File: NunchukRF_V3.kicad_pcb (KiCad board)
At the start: 2 copper layers, 26.9 x 46.7 mm, 43 parts, among them K1 Buttons, P1 V+, P2 V-, P3 D-, P4 Vbat-, P5 Vbat+, P6 D+, Q1 MOSFET_N, Q2 MOSFET_P, U1 STM32F100C6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

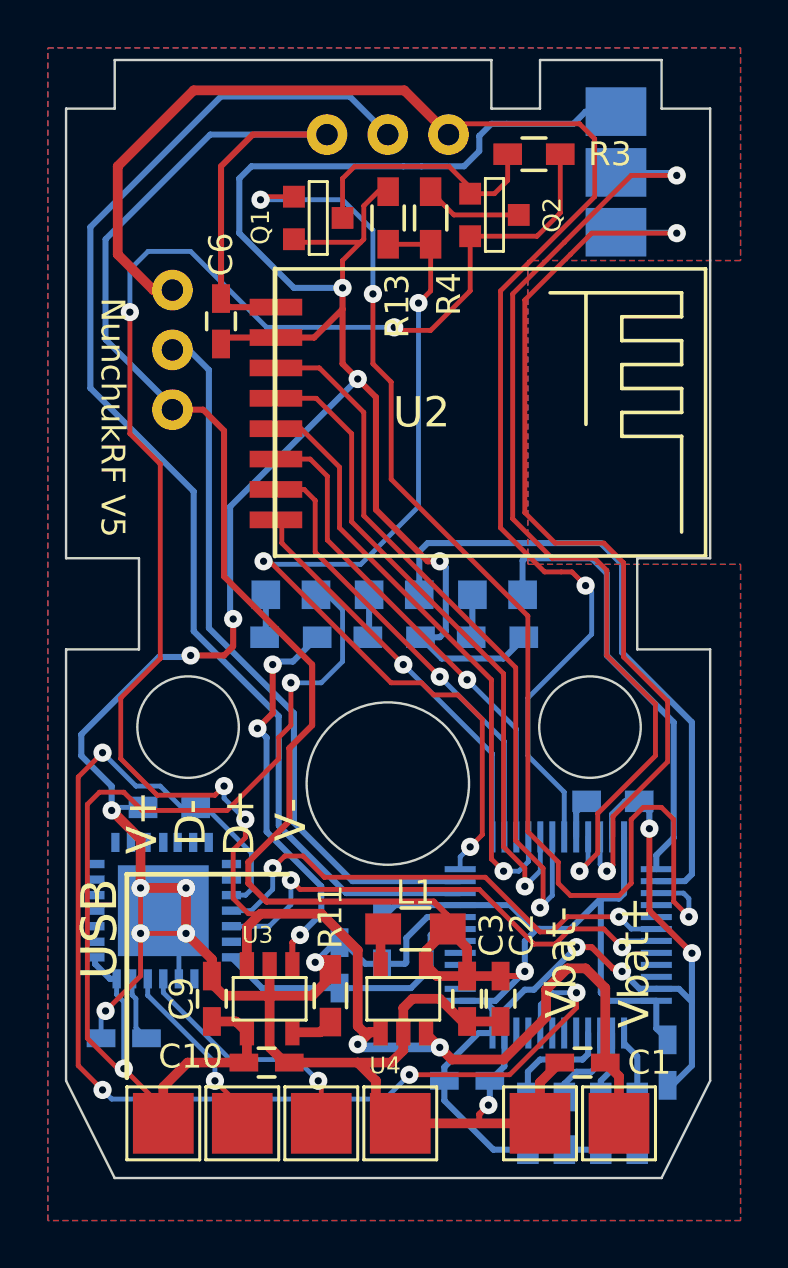
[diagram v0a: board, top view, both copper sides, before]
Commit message: Added cp2102 power detect connection to mcu
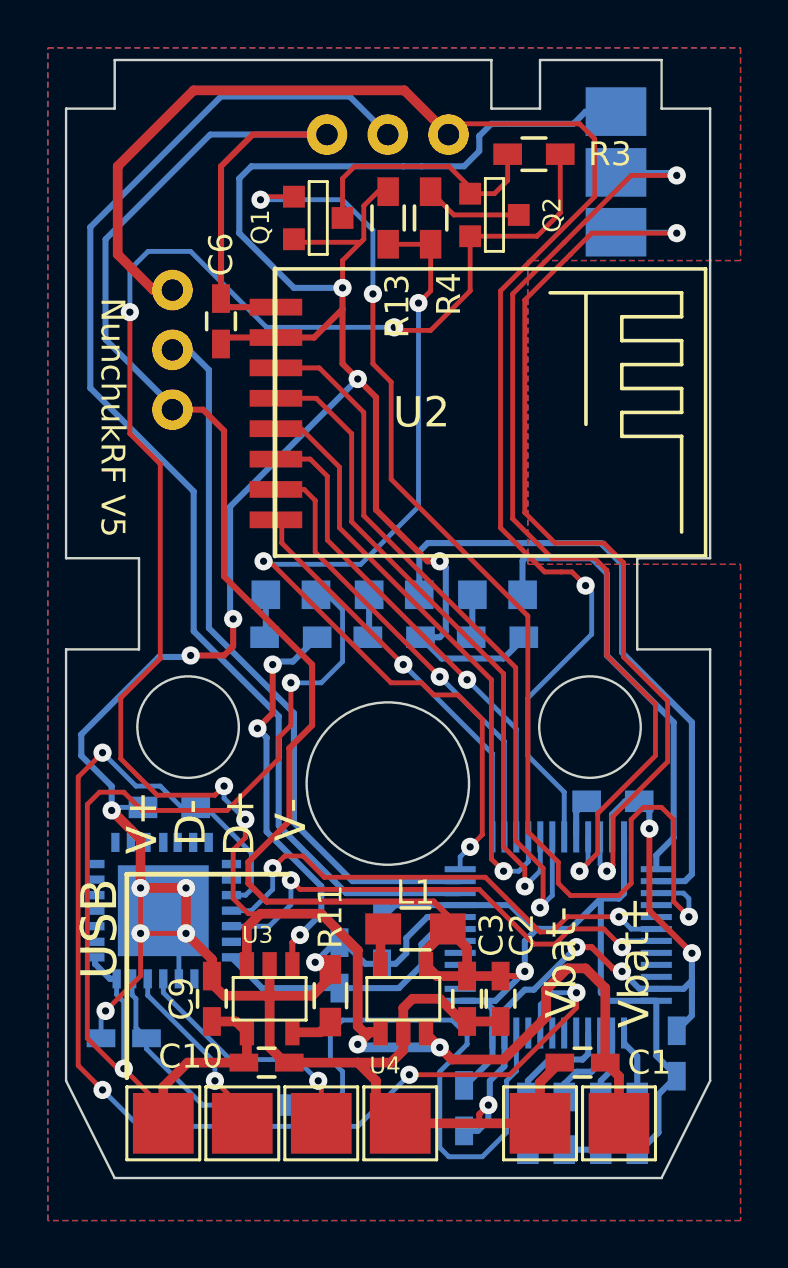
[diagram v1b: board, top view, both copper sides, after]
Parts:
- added R14: 2k, Resistors_SMD:R_0603_HandSoldering, B.Cu at (224.3, 88.4)
- moved C7 1.15 mm to (232.5, 88.5), turned to 90 degrees
- moved C5 0.54 mm to (241.4, 86.2), turned to 270 degrees
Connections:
- net Net-(C11-Pad2) renamed CP2102_ON
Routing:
- net Net-(R14-Pad2): track 0.00 -> 24.1 mm
- net CP2102_ON: track 2.73 -> 8.07 mm
- net GND: track 193.2 -> 192.2 mm
- net BOOT0: track 50.4 -> 51.4 mm
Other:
- board text added: "Addr b0 - b3"
- board text removed: "Address b0 - b3"

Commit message: Updated NRF labels
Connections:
- U1 pad 13: NRF_CE -> NRF_IRQ
- U1 pad 14: NRF_CSN -> NRF_MISO
- U1 pad 15: NRF_SCK -> NRF_MOSI
- U1 pad 16: NRF_MOSI -> NRF_SCK
- U1 pad 17: NRF_MISO -> NRF_CSN
- U1 pad 18: NRF_IRQ -> NRF_CE
- U1 pad 2: Net-(U1-Pad2) -> (no net)
- U1 pad 28: Net-(U1-Pad28) -> (no net)
- U1 pad 29: Net-(U1-Pad29) -> (no net)
- U1 pad 3: Net-(U1-Pad3) -> (no net)
- U1 pad 32: Net-(U1-Pad32) -> (no net)
- U1 pad 33: Net-(U1-Pad33) -> (no net)
- U1 pad 34: Net-(U1-Pad34) -> (no net)
- U1 pad 4: Net-(U1-Pad4) -> (no net)
- U1 pad 41: Net-(U1-Pad41) -> (no net)
- U1 pad 42: Net-(U1-Pad42) -> (no net)
- U1 pad 43: Net-(U1-Pad43) -> (no net)
- U1 pad 45: Net-(U1-Pad45) -> (no net)
- U1 pad 5: Net-(U1-Pad5) -> (no net)
- U1 pad 6: Net-(U1-Pad6) -> (no net)
- U2 pad 3: NRF_IRQ -> NRF_CE
- U2 pad 4: NRF_MISO -> NRF_CSN
- U2 pad 5: NRF_MOSI -> NRF_SCK
- U2 pad 6: NRF_SCK -> NRF_MOSI
- U2 pad 7: NRF_CSN -> NRF_MISO
- U2 pad 8: NRF_CE -> NRF_IRQ
- U5 pad 1: Net-(U5-Pad1) -> (no net)
- U5 pad 11: Net-(U5-Pad11) -> (no net)
- U5 pad 12: Net-(U5-Pad12) -> (no net)
- U5 pad 18: Net-(U5-Pad18) -> (no net)
- U5 pad 2: Net-(U5-Pad2) -> (no net)
- U5 pad 23: Net-(U5-Pad23) -> (no net)
- U5 pad 27: Net-(U5-Pad27) -> (no net)
- U5 pad 9: Net-(U5-Pad9) -> (no net)
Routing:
- net NRF_CE: track 17.0 -> 31.5 mm
- net NRF_IRQ: track 31.5 -> 17.0 mm
- net NRF_MISO: track 28.0 -> 19.2 mm
- net NRF_CSN: track 19.2 -> 28.0 mm
- net NRF_SCK: track 20.8 -> 25.3 mm
- net NRF_MOSI: track 25.3 -> 20.8 mm

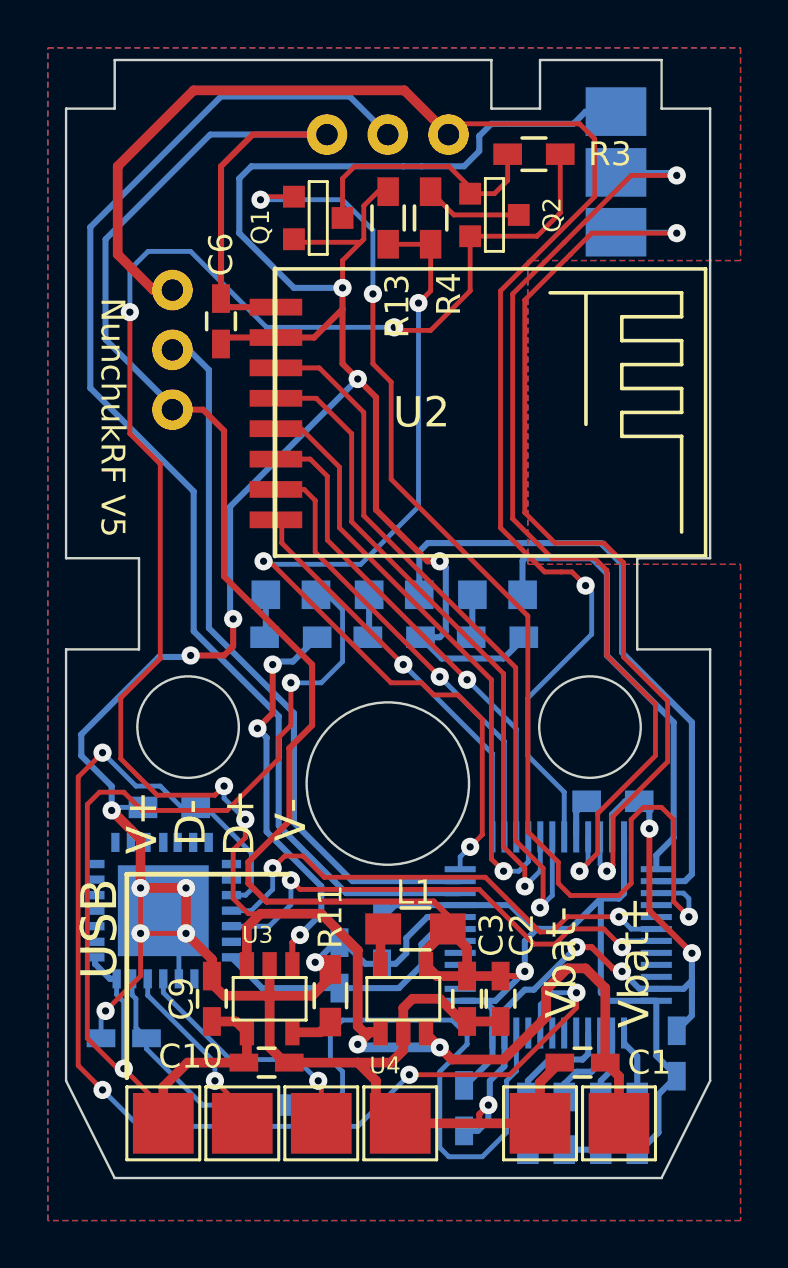
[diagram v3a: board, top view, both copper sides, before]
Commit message: Changed CP2102 footprint
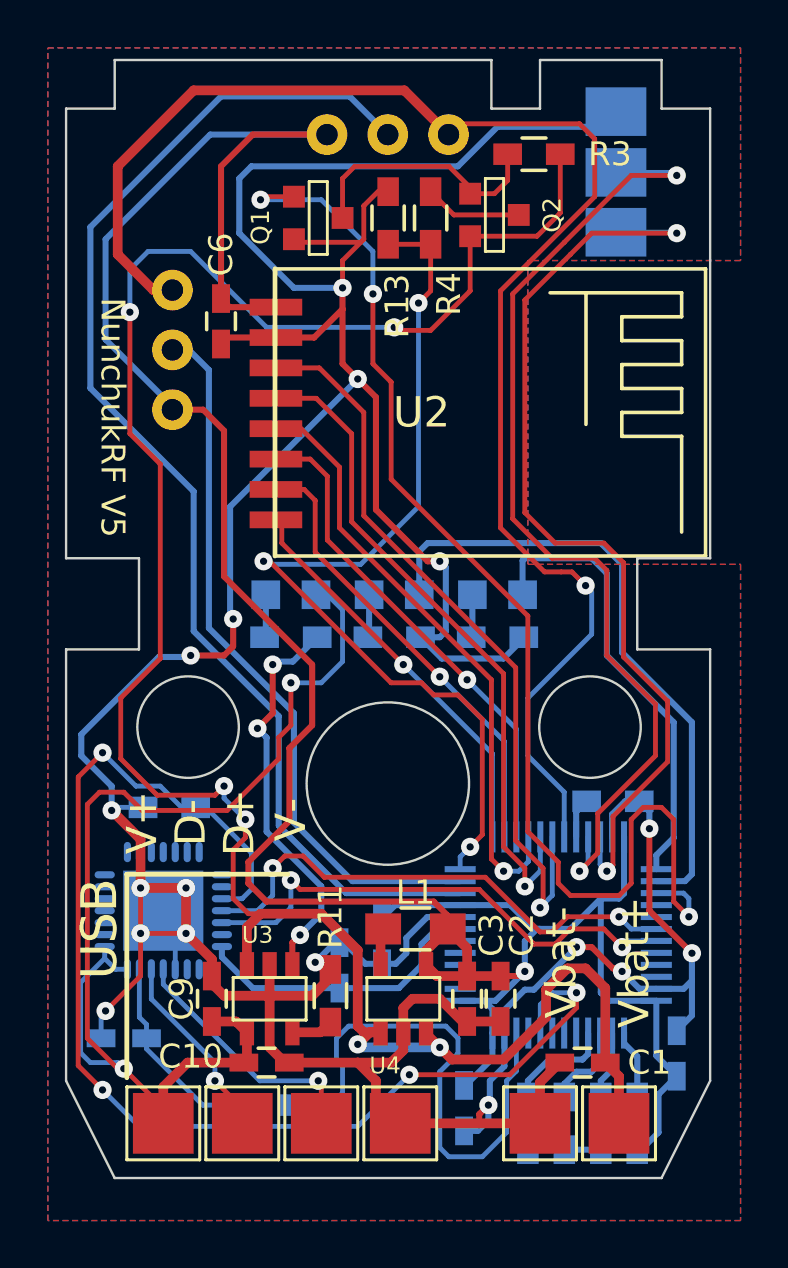
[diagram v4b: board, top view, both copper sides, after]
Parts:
- U5: footprint w_smd_qfn:qfn-28 -> Housings_DFN_QFN:QFN-28-1EP_5x5mm_Pitch0.5mm
- turned U5 to 90 degrees
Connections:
- U1 pad 2: (no net) -> Net-(U1-Pad2)
- U1 pad 28: (no net) -> Net-(U1-Pad28)
- U1 pad 29: (no net) -> Net-(U1-Pad29)
- U1 pad 3: (no net) -> Net-(U1-Pad3)
- U1 pad 32: (no net) -> Net-(U1-Pad32)
- U1 pad 33: (no net) -> Net-(U1-Pad33)
- U1 pad 34: (no net) -> Net-(U1-Pad34)
- U1 pad 4: (no net) -> Net-(U1-Pad4)
- U1 pad 41: (no net) -> Net-(U1-Pad41)
- U1 pad 42: (no net) -> Net-(U1-Pad42)
- U1 pad 43: (no net) -> Net-(U1-Pad43)
- U1 pad 45: (no net) -> Net-(U1-Pad45)
- U1 pad 5: (no net) -> Net-(U1-Pad5)
- U1 pad 6: (no net) -> Net-(U1-Pad6)
- U5 pad 1: (no net) -> Net-(U5-Pad1)
- U5 pad 11: (no net) -> Net-(U5-Pad11)
- U5 pad 12: (no net) -> Net-(U5-Pad12)
- U5 pad 18: (no net) -> Net-(U5-Pad18)
- U5 pad 2: (no net) -> Net-(U5-Pad2)
- U5 pad 23: (no net) -> Net-(U5-Pad23)
- U5 pad 27: (no net) -> Net-(U5-Pad27)
- U5 pad 9: (no net) -> Net-(U5-Pad9)
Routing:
- net V_IN: track 47.3 -> 50.0 mm
- net Net-(R14-Pad2): track 24.1 -> 22.8 mm
- net RESET: track 11.6 -> 12.5 mm
- net TX_BOOT: track 21.0 -> 21.6 mm
- net BATT_MEASURE_ON: track 52.1 -> 51.5 mm
- net GND: track 192.2 -> 192.7 mm

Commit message: Small update
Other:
- board text added: "+"
- board text added: "-"
- board text added: "D+"
- board text added: "D-"
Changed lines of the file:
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@@
     (area 215.0116 44.196 244.2544 93.218001)
     (thickness 1.6)
-    (drawings 43)
+    (drawings 49)
     (tracks 665)
     (zones 0)
@@
     (pad_to_mask_clearance 0)
     (aux_axis_origin 0 0)
-    (visible_elements 7FFFFF7F)
+    (visible_elements 7FFFFFFF)
     (pcbplotparams
       (layerselection 0x010f0_80000001)
@@
       (effects (font (thickness 0.3048)))
     )
-    (fp_text value V+ (at -0.889 -12.573 90) (layer F.SilkS)
+    (fp_text value V+ (at -0.889 -12.573 90) (layer F.SilkS) hide
       (effects (font (thickness 0.3048)))
     )
@@
       (effects (font (thickness 0.3048)))
     )
-    (fp_text value V- (at -4.572 -12.7 270) (layer F.SilkS)
+    (fp_text value V- (at -4.572 -12.7 90) (layer F.SilkS) hide
       (effects (font (thickness 0.3048)))
     )
@@
       (effects (font (thickness 0.3048)))
     )
-    (fp_text value D- (at -2.159 -12.573 90) (layer F.SilkS)
+    (fp_text value D- (at -2.159 -12.573 90) (layer F.SilkS) hide
       (effects (font (thickness 0.3048)))
     )
@@
       (effects (font (thickness 0.3048)))
     )
-    (fp_text value Vbat- (at 0.889 -6.731 90) (layer F.SilkS)
+    (fp_text value Vbat- (at 0.889 -6.731 90) (layer F.SilkS) hide
       (effects (font (thickness 0.3048)))
     )
@@
       (effects (font (thickness 0.3048)))
     )
-    (fp_text value Vbat+ (at 0.635 -6.731 90) (layer F.SilkS)
+    (fp_text value Vbat+ (at 0.635 -6.731 90) (layer F.SilkS) hide
       (effects (font (thickness 0.3048)))
     )
@@
       (effects (font (thickness 0.3048)))
     )
-    (fp_text value D+ (at -3.429 -12.573 90) (layer F.SilkS)
+    (fp_text value D+ (at -3.429 -12.573 90) (layer F.SilkS) hide
       (effects (font (thickness 0.3048)))
     )
@@
     )
   )
+  (gr_text D+ (at 223.012 76.835 90) (layer F.SilkS)
+    (effects (font (size 1.5 1.5) (thickness 0.3)))
+  )
+  (gr_text D- (at 220.98 76.835 90) (layer F.SilkS)
+    (effects (font (size 1.5 1.5) (thickness 0.3)))
+  )
+  (gr_text - (at 224.663 77.47 90) (layer F.SilkS)
+    (effects (font (size 1.5 1.5) (thickness 0.3)))
+  )
+  (gr_text + (at 218.821 77.597 90) (layer F.SilkS)
+    (effects (font (size 1.5 1.5) (thickness 0.3)))
+  )
+  (gr_text - (at 235.712 84.836) (layer F.SilkS)
+    (effects (font (size 1.5 1.5) (thickness 0.3)))
+  )
+  (gr_text + (at 239.141 84.709) (layer F.SilkS)
+    (effects (font (size 1.5 1.5) (thickness 0.3)))
+  )
   (gr_circle (center 222.885 83.693) (end 223.139 83.947) (layer B.SilkS) (width 0.2))

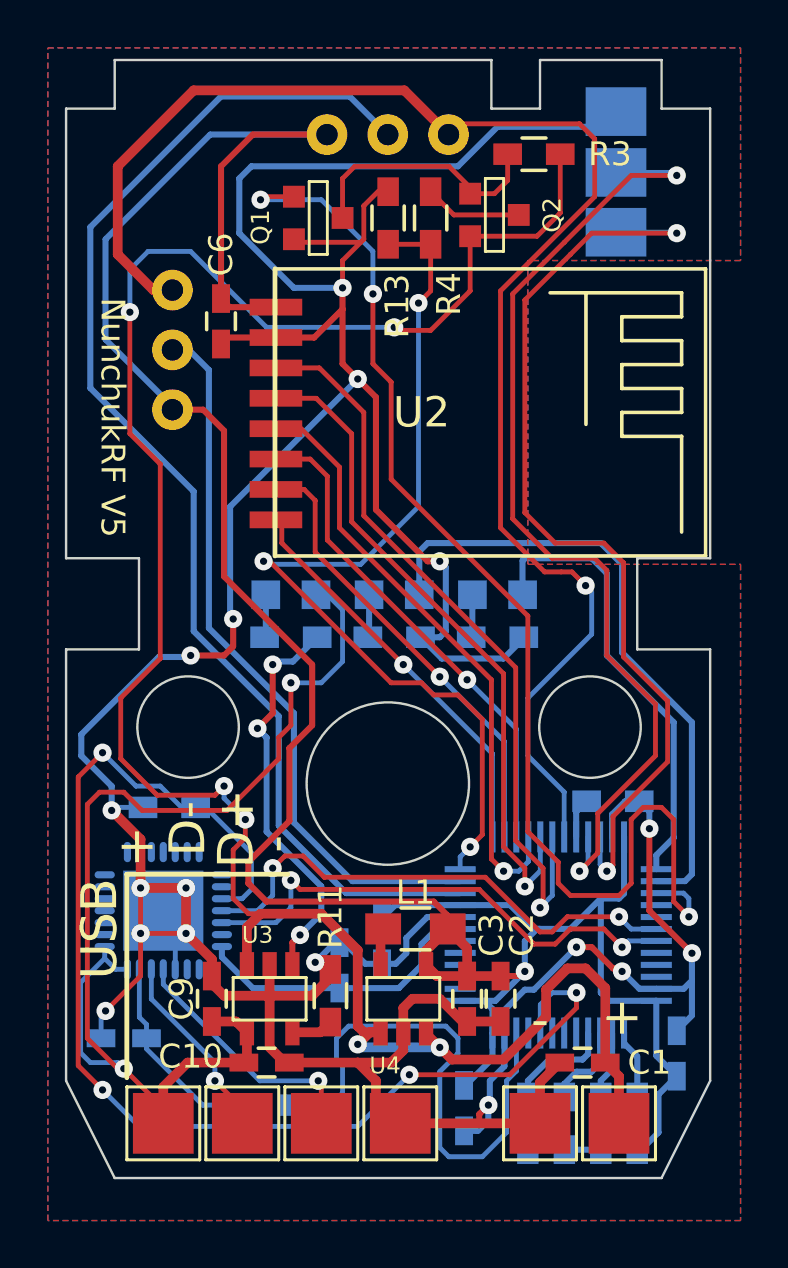
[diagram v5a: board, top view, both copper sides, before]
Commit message: Moved nrf, changed button connector, updated labels
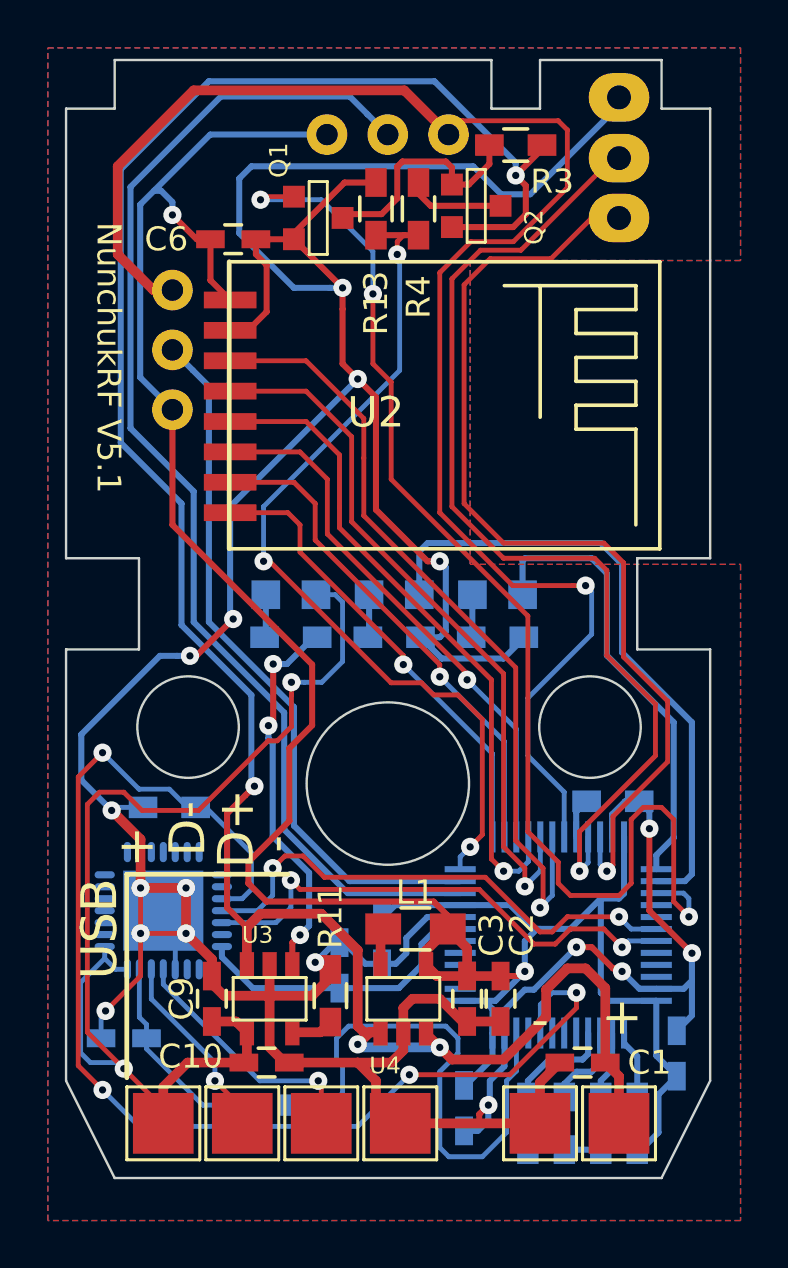
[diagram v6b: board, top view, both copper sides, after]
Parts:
- D1: value LED -> RED
- D2: value LED -> GREEN
- D3: value LED -> BLUE
- moved C6 3.47 mm to (222.9, 52.2), turned to 180 degrees
- moved U2 1.94 mm to (228.7, 59.1)
- moved Q2 0.85 mm to (233.0, 50.8)
- moved R3 0.85 mm to (234.7, 48.3)
- moved R13 0.63 mm to (228.9, 50.9)
- moved R4 0.63 mm to (230.6, 50.9)
- moved K1 0.61 mm to (239.0, 48.8)
- turned D1 to 0 degrees
- turned D2 to 0 degrees
- turned D3 to 0 degrees
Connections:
- U1 pad 2: Net-(U1-Pad2) -> (no net)
- U1 pad 28: Net-(U1-Pad28) -> (no net)
- U1 pad 29: Net-(U1-Pad29) -> (no net)
- U1 pad 3: Net-(U1-Pad3) -> (no net)
- U1 pad 32: Net-(U1-Pad32) -> (no net)
- U1 pad 33: Net-(U1-Pad33) -> (no net)
- U1 pad 34: Net-(U1-Pad34) -> (no net)
- U1 pad 4: Net-(U1-Pad4) -> (no net)
- U1 pad 41: Net-(U1-Pad41) -> (no net)
- U1 pad 42: Net-(U1-Pad42) -> (no net)
- U1 pad 43: Net-(U1-Pad43) -> (no net)
- U1 pad 45: Net-(U1-Pad45) -> (no net)
- U1 pad 5: Net-(U1-Pad5) -> (no net)
- U1 pad 6: Net-(U1-Pad6) -> (no net)
- U5 pad 1: Net-(U5-Pad1) -> (no net)
- U5 pad 11: Net-(U5-Pad11) -> (no net)
- U5 pad 12: Net-(U5-Pad12) -> (no net)
- U5 pad 18: Net-(U5-Pad18) -> (no net)
- U5 pad 2: Net-(U5-Pad2) -> (no net)
- U5 pad 23: Net-(U5-Pad23) -> (no net)
- U5 pad 27: Net-(U5-Pad27) -> (no net)
- U5 pad 9: Net-(U5-Pad9) -> (no net)
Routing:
- net VCC: track 116.2 -> 107.5 mm, vias 1 -> 2
- net +BATT: track 91.4 -> 94.3 mm, vias 6 -> 4
- net NRF_IRQ: track 17.0 -> 19.8 mm
- net CHUK_P_GND: track 64.4 -> 67.1 mm
- net BATT_MEASURE: track 39.0 -> 36.5 mm
- net NRF_SCK: track 25.3 -> 27.6 mm
- net NRF_MOSI: track 20.8 -> 22.8 mm
- net NRF_MISO: track 19.2 -> 21.1 mm
- net NRF_CSN: track 28.0 -> 30.0 mm
- net NRF_CE: track 31.5 -> 33.4 mm
- net GND: track 192.7 -> 194.2 mm
- net CHUK_P1_C: track 52.4 -> 51.0 mm
- net CHUK_BT_C: track 40.2 -> 41.4 mm, vias 2 -> 1
- net Net-(Q1-PadD): track 10.7 -> 9.86 mm
- net Net-(R12-Pad2): track 16.8 -> 16.0 mm
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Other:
- board text added: "NunchukRF V5.1"
- board text removed: "NunchukRF V5"
